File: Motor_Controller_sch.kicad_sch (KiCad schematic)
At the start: 61 parts, among them J1 1988804, J10 1988862, J11 Barrel_Jack_Switch, J12 +5V, J13 1988862, J14 1988817, J2 GND, J3 RX, J4 TX, J5 RESET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

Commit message: Updated all relevent files for repo
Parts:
- removed TP14, TP15: TestPoint, TestPoint:TestPoint_THTPad_1.0x1.0mm_Drill0.5mm, symbol Connector:TestPoint
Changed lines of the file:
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@@
 	)
 	(junction
-		(at 228.6 85.09)
-		(diameter 0)
-		(color 0 0 0 0)
-	)
-	(junction
 		(at 193.04 57.15)
 		(diameter 0)
@@
 	(wire
 		(pts
-			(xy 228.6 82.55) (xy 228.6 85.09)
+			(xy 228.6 82.55) (xy 228.6 88.9)
 		)
 		(stroke
@@
 	(wire
 		(pts
-			(xy 228.6 85.09) (xy 228.6 88.9)
-		)
-		(stroke
-			(width 0)
-			(type default)
-		)
-	)
-	(wire
-		(pts
 			(xy 43.18 24.13) (xy 43.18 26.67)
 		)
@@
 	)
 	(symbol
-		(lib_id "Connector:TestPoint")
-		(at 59.69 106.68 270)
-		(unit 1)
-		(exclude_from_sim no)
-		(in_bom yes)
-		(on_board yes)
-		(dnp no)
-		(fields_autoplaced yes)
-		(property "Reference" "TP14"
-			(at 64.77 106.6799 90)
-			(effects
-				(font
-					(size 1.27 1.27)
-				)
-				(justify left)
-			)
-		)
-		(property "Value" "TestPoint"
-			(at 61.7221 109.22 0)
-			(effects
-				(font
-					(size 1.27 1.27)
-				)
-				(justify left)
-				(hide yes)
-			)
-		)
-		(property "Footprint" "TestPoint:TestPoint_THTPad_1.0x1.0mm_Drill0.5mm"
-			(at 59.69 111.76 0)
-			(effects
-				(font
-					(size 1.27 1.27)
-				)
-				(hide yes)
-			)
-		)
-		(property "Datasheet" "~"
-			(at 59.69 111.76 0)
-			(effects
-				(font
-					(size 1.27 1.27)
-				)
-				(hide yes)
-			)
-		)
-		(property "Description" "test point"
-			(at 59.69 106.68 0)
-			(effects
-				(font
-					(size 1.27 1.27)
-				)
-				(hide yes)
-			)
-		)
-		(pin "1"
-		)
-		(instances
-			(project "SuperCapacitorBike"
-				(path "/1096cbe7-ac56-48cb-aadd-3e4addcdbbb7/a964da0d-002d-40d7-a8b6-c48f0e32c7fd"
-					(reference "TP14")
-					(unit 1)
-				)
-			)
-		)
-	)
-	(symbol
 		(lib_id "power:GND")
 		(at 121.92 180.34 0)
@@
 	)
 	(symbol
-		(lib_id "power:PWR_FLAG")
-		(at 228.6 85.09 90)
-		(unit 1)
-		(exclude_from_sim no)
-		(in_bom yes)
-		(on_board yes)
-		(dnp no)
-		(fields_autoplaced yes)
-		(property "Reference" "#FLG07"
-			(at 226.695 85.09 0)
-			(effects
-				(font
-					(size 1.27 1.27)
-				)
-				(hide yes)
-			)
-		)
-		(property "Value" "PWR_FLAG"
-			(at 224.79 85.0899 90)
-			(effects
-				(font
-					(size 1.27 1.27)
-				)
-				(justify left)
-			)
-		)
-		(property "Footprint" ""
-			(at 228.6 85.09 0)
-			(effects
-				(font
-					(size 1.27 1.27)
-				)
-				(hide yes)
-			)
-		)
-		(property "Datasheet" "~"
-			(at 228.6 85.09 0)
-			(effects
-				(font
-					(size 1.27 1.27)
-				)
-				(hide yes)
-			)
-		)
-		(property "Description" "Special symbol for telling ERC where power comes from"
-			(at 228.6 85.09 0)
-			(effects
-				(font
-					(size 1.27 1.27)
-				)
-				(hide yes)
-			)
-		)
-		(pin "1"
-		)
-		(instances
-			(project "SuperCapacitorBike"
-				(path "/1096cbe7-ac56-48cb-aadd-3e4addcdbbb7/a964da0d-002d-40d7-a8b6-c48f0e32c7fd"
-					(reference "#FLG07")
-					(unit 1)
-				)
-			)
-		)
-	)
-	(symbol
 		(lib_id "Device:C_Small")
 		(at 128.27 55.88 180)
@@
 					(unit 1)
 				)
-			)
-		)
-	)
-	(symbol
-		(lib_id "Connector:TestPoint")
-		(at 59.69 109.22 270)
-		(unit 1)
-		(exclude_from_sim no)
-		(in_bom yes)
-		(on_board yes)
-		(dnp no)
-		(fields_autoplaced yes)
-		(property "Reference" "TP15"
-			(at 64.77 109.2199 90)
-			(effects
-				(font
-					(size 1.27 1.27)
-				)
-				(justify left)
-			)
-		)
-		(property "Value" "TestPoint"
-			(at 61.7221 111.76 0)
-			(effects
-				(font
-					(size 1.27 1.27)
-				)
-				(justify left)
-				(hide yes)
-			)
-		)
-		(property "Footprint" "TestPoint:TestPoint_THTPad_1.0x1.0mm_Drill0.5mm"
-			(at 59.69 114.3 0)
-			(effects
-				(font
-					(size 1.27 1.27)
-				)
-				(hide yes)
-			)
-		)
-		(property "Datasheet" "~"
-			(at 59.69 114.3 0)
-			(effects
-				(font
-					(size 1.27 1.27)
-				)
-				(hide yes)
-			)
-		)
-		(property "Description" "test point"
-			(at 59.69 109.22 0)
-			(effects
-				(font
-					(size 1.27 1.27)
-				)
-				(hide yes)
-			)
-		)
-		(pin "1"
-		)
-		(instances
-			(project "SuperCapacitorBike"
-				(path "/1096cbe7-ac56-48cb-aadd-3e4addcdbbb7/a964da0d-002d-40d7-a8b6-c48f0e32c7fd"
-					(reference "TP15")
-					(unit 1)
-				)

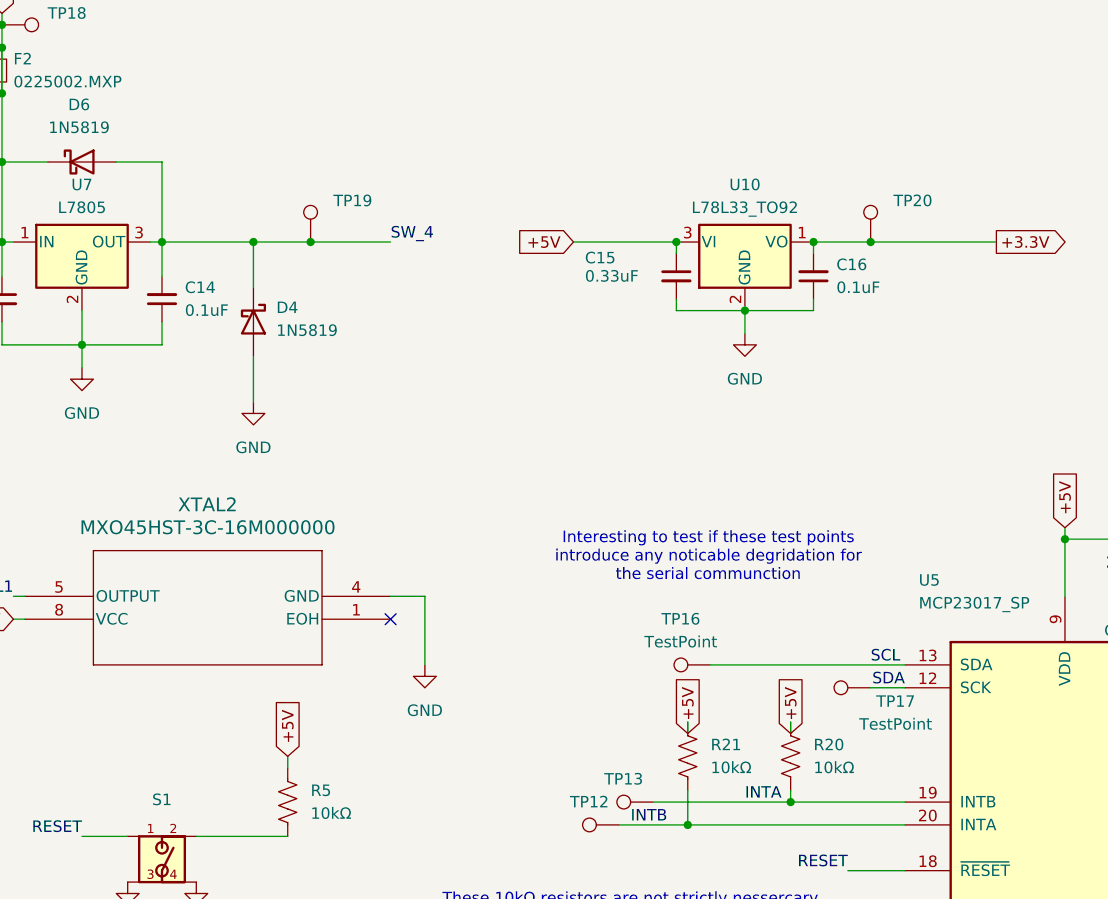
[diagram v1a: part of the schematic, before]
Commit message: Fixed I2C error
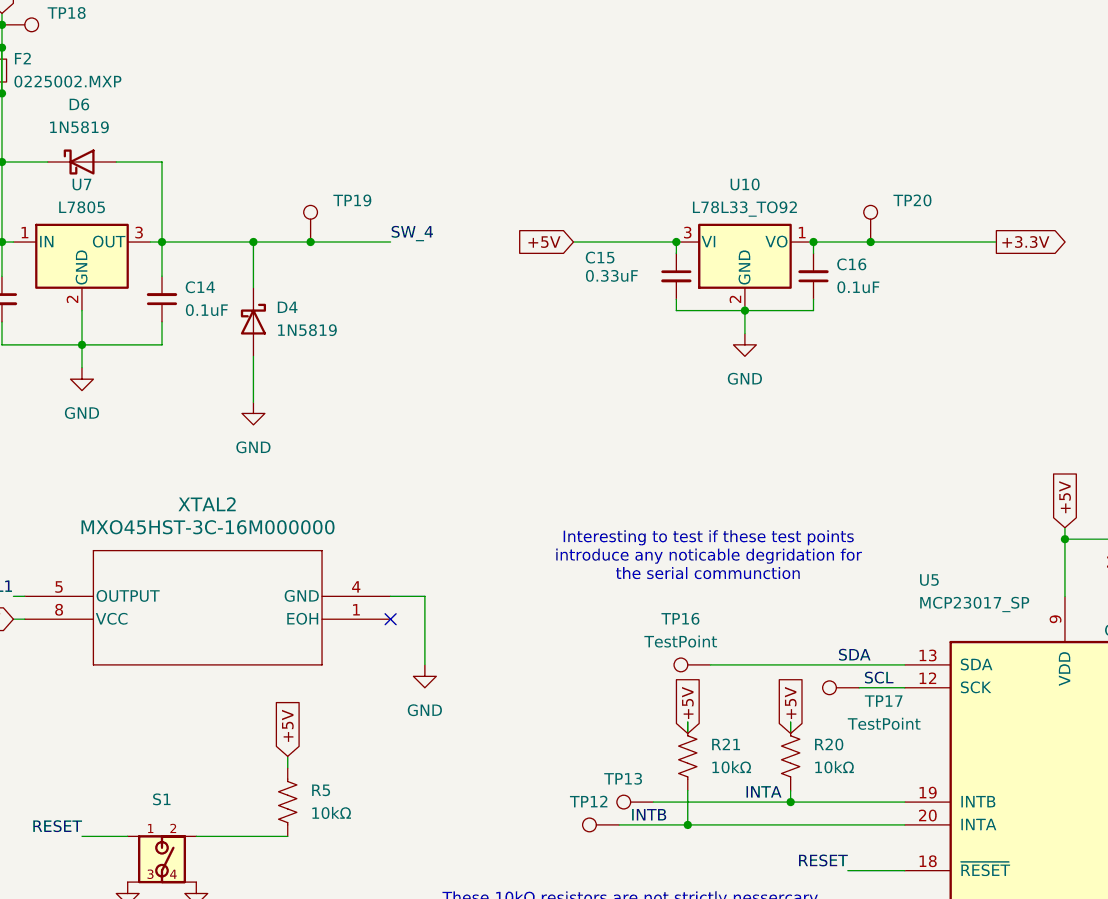
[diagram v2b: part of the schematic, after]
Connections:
- net SCL: now also TP17.1, U5.12 (SCK); no longer TP16.1, U5.13 (SDA)
- net SDA: now also TP16.1, U5.13 (SDA); no longer TP17.1, U5.12 (SCK)
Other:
- moved on the sheet: TP17
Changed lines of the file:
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@@
 	(wire
 		(pts
-			(xy 210.82 99.06) (xy 207.01 99.06)
-		)
-		(stroke
-			(width 0)
-			(type default)
-		)
-	)
-	(wire
-		(pts
 			(xy 270.51 101.6) (xy 275.59 101.6)
 		)
@@
 	(wire
 		(pts
-			(xy 189.23 96.52) (xy 210.82 96.52)
-		)
-		(stroke
-			(width 0)
-			(type default)
-		)
-	)
-	(wire
-		(pts
 			(xy 207.01 49.53) (xy 220.98 49.53)
 		)
@@
 	(wire
 		(pts
+			(xy 128.27 40.64) (xy 128.27 49.53)
+		)
+		(stroke
+			(width 0)
+			(type default)
+		)
+	)
+	(wire
+		(pts
 			(xy 157.48 96.52) (xy 157.48 88.9)
 		)
@@
 	(wire
 		(pts
+			(xy 189.23 96.52) (xy 210.82 96.52)
+		)
+		(stroke
+			(width 0)
+			(type default)
+		)
+	)
+	(wire
+		(pts
 			(xy 82.55 176.53) (xy 82.55 180.34)
 		)
@@
 	(wire
 		(pts
-			(xy 128.27 49.53) (xy 128.27 40.64)
-		)
-		(stroke
-			(width 0)
-			(type default)
-		)
-	)
-	(wire
-		(pts
 			(xy 246.38 99.06) (xy 257.81 99.06)
 		)
@@
 	(wire
 		(pts
+			(xy 205.74 99.06) (xy 210.82 99.06)
+		)
+		(stroke
+			(width 0)
+			(type default)
+		)
+	)
+	(wire
+		(pts
 			(xy 92.71 176.53) (xy 92.71 187.96)
 		)
@@
 		)
 	)
-	(label "SDA"
-		(at 210.82 99.06 180)
-		(fields_autoplaced yes)
-		(effects
-			(font
-				(size 1.27 1.27)
-			)
-			(justify right bottom)
-		)
-	)
 	(label "BRK2"
 		(at 250.19 127 0)
@@
 		)
 	)
-	(label "SCL"
-		(at 207.01 96.52 0)
+	(label "SDA"
+		(at 207.01 96.52 180)
 		(fields_autoplaced yes)
 		(effects
@@
 				(size 1.27 1.27)
 			)
-			(justify left bottom)
+			(justify right bottom)
 		)
 	)
@@
 		)
 	)
+	(label "SCL"
+		(at 209.55 99.06 180)
+		(fields_autoplaced yes)
+		(effects
+			(font
+				(size 1.27 1.27)
+			)
+			(justify right bottom)
+		)
+	)
 	(label "XTAL1"
 		(at 63.5 78.74 0)
@@
 	(symbol
 		(lib_id "Connector:TestPoint")
-		(at 207.01 99.06 90)
+		(at 205.74 99.06 90)
 		(unit 1)
 		(exclude_from_sim no)
@@
 		(dnp no)
 		(property "Reference" "TP17"
-			(at 209.804 100.584 90)
+			(at 208.534 100.584 90)
 			(effects
 				(font
@@
 		)
 		(property "Value" "TestPoint"
-			(at 209.804 103.124 90)
+			(at 208.534 103.124 90)
 			(effects
 				(font
@@
 		)
 		(property "Footprint" "TestPoint:TestPoint_THTPad_1.0x1.0mm_Drill0.5mm"
-			(at 207.01 93.98 0)
+			(at 205.74 93.98 0)
 			(effects
 				(font
@@
 		)
 		(property "Datasheet" "~"
-			(at 207.01 93.98 0)
+			(at 205.74 93.98 0)
 			(effects
 				(font
@@
 		)
 		(property "Description" "test point"
-			(at 207.01 99.06 0)
+			(at 205.74 99.06 0)
 			(effects
 				(font
